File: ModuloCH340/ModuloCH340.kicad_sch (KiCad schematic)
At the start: 20 parts, among them J1001 USB_C_Receptacle_USB2.0, J1002 USB_B, J1003 Conn_01x04, U1001 CH340G, Y1001 12Mhz

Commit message: Some changes in arduino board.
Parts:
- renumbered C1001 to C13, C1002 to C14, C1003 to C15, C1004 to C16, D1001 to D3, D1002 to D4, J1001 to J11, J1002 to J12, J1003 to J13, JP1001 to JP1, R1006 to R10, R1007 to R11, R1008 to R12, R1001 to R5, R1002 to R6, R1003 to R7, R1004 to R8, R1005 to R9, U1001 to U3, Y1001 to Y2
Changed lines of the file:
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@@
 		(on_board yes)
 		(dnp no)
-		(property "Reference" "R1007"
+		(property "Reference" "R11"
 			(at 201.422 115.824 0)
 			(effects
@@
 				)
 			)
+			(project "ModuloCH340"
+				(path "/b1260de1-9c48-4b08-a759-f31e40d6183e/17bee45f-f3a2-49e1-a0f6-7717cbcaab1c"
+					(reference "R11")
+					(unit 1)
+				)
+			)
 		)
 	)
@@
 		(dnp no)
 		(fields_autoplaced yes)
-		(property "Reference" "R1002"
+		(property "Reference" "R6"
 			(at 121.92 76.1999 0)
 			(effects
@@
 				)
 			)
+			(project "ModuloCH340"
+				(path "/b1260de1-9c48-4b08-a759-f31e40d6183e/17bee45f-f3a2-49e1-a0f6-7717cbcaab1c"
+					(reference "R6")
+					(unit 1)
+				)
+			)
 		)
 	)
@@
 		(dnp no)
 		(fields_autoplaced yes)
-		(property "Reference" "R1001"
+		(property "Reference" "R5"
 			(at 113.03 76.1999 0)
 			(effects
@@
 				)
 			)
+			(project ""
+				(path "/b1260de1-9c48-4b08-a759-f31e40d6183e/17bee45f-f3a2-49e1-a0f6-7717cbcaab1c"
+					(reference "R5")
+					(unit 1)
+				)
+			)
 		)
 	)
@@
 		(on_board yes)
 		(dnp no)
-		(property "Reference" "Y1001"
+		(property "Reference" "Y2"
 			(at 125.476 118.11 0)
 			(effects
@@
 				(path "/49c4e1fc-25c5-4450-b617-b77ec3b06c82"
 					(reference "Y1001")
+					(unit 1)
+				)
+			)
+			(project ""
+				(path "/b1260de1-9c48-4b08-a759-f31e40d6183e/17bee45f-f3a2-49e1-a0f6-7717cbcaab1c"
+					(reference "Y2")
 					(unit 1)
 				)
@@
 		(dnp no)
 		(fields_autoplaced yes)
-		(property "Reference" "C1003"
+		(property "Reference" "C15"
 			(at 168.91 68.5862 0)
 			(effects
@@
 				)
 			)
+			(project ""
+				(path "/b1260de1-9c48-4b08-a759-f31e40d6183e/17bee45f-f3a2-49e1-a0f6-7717cbcaab1c"
+					(reference "C15")
+					(unit 1)
+				)
+			)
 		)
 	)
@@
 		(on_board yes)
 		(dnp no)
-		(property "Reference" "C1001"
+		(property "Reference" "C13"
 			(at 123.698 127.508 0)
 			(effects
@@
 				)
 			)
+			(project "ModuloCH340"
+				(path "/b1260de1-9c48-4b08-a759-f31e40d6183e/17bee45f-f3a2-49e1-a0f6-7717cbcaab1c"
+					(reference "C13")
+					(unit 1)
+				)
+			)
 		)
 	)
@@
 		(dnp no)
 		(fields_autoplaced yes)
-		(property "Reference" "C1004"
+		(property "Reference" "C16"
 			(at 214.63 80.0162 0)
 			(effects
@@
 				)
 			)
+			(project "ModuloCH340"
+				(path "/b1260de1-9c48-4b08-a759-f31e40d6183e/17bee45f-f3a2-49e1-a0f6-7717cbcaab1c"
+					(reference "C16")
+					(unit 1)
+				)
+			)
 		)
 	)
@@
 		(dnp no)
 		(fields_autoplaced yes)
-		(property "Reference" "R1005"
+		(property "Reference" "R9"
 			(at 185.42 85.09 90)
 			(effects
@@
 				)
 			)
+			(project "ModuloCH340"
+				(path "/b1260de1-9c48-4b08-a759-f31e40d6183e/17bee45f-f3a2-49e1-a0f6-7717cbcaab1c"
+					(reference "R9")
+					(unit 1)
+				)
+			)
 		)
 	)
@@
 		(dnp no)
 		(fields_autoplaced yes)
-		(property "Reference" "J1003"
+		(property "Reference" "J13"
 			(at 180.34 100.3299 0)
 			(effects
@@
 				)
 			)
+			(project ""
+				(path "/b1260de1-9c48-4b08-a759-f31e40d6183e/17bee45f-f3a2-49e1-a0f6-7717cbcaab1c"
+					(reference "J13")
+					(unit 1)
+				)
+			)
 		)
 	)
@@
 		(on_board yes)
 		(dnp no)
-		(property "Reference" "R1004"
+		(property "Reference" "R8"
 			(at 132.08 102.87 90)
 			(effects
@@
 				)
 			)
+			(project "ModuloCH340"
+				(path "/b1260de1-9c48-4b08-a759-f31e40d6183e/17bee45f-f3a2-49e1-a0f6-7717cbcaab1c"
+					(reference "R8")
+					(unit 1)
+				)
+			)
 		)
 	)
@@
 		(dnp no)
 		(fields_autoplaced yes)
-		(property "Reference" "J1001"
+		(property "Reference" "J11"
 			(at 83.82 57.15 0)
 			(effects
@@
 				)
 			)
+			(project ""
+				(path "/b1260de1-9c48-4b08-a759-f31e40d6183e/17bee45f-f3a2-49e1-a0f6-7717cbcaab1c"
+					(reference "J11")
+					(unit 1)
+				)
+			)
 		)
 	)
@@
 		(dnp no)
 		(fields_autoplaced yes)
-		(property "Reference" "J1002"
+		(property "Reference" "J12"
 			(at 88.9 109.22 0)
 			(effects
@@
 				)
 			)
+			(project ""
+				(path "/b1260de1-9c48-4b08-a759-f31e40d6183e/17bee45f-f3a2-49e1-a0f6-7717cbcaab1c"
+					(reference "J12")
+					(unit 1)
+				)
+			)
 		)
 	)
@@
 		(dnp no)
 		(fields_autoplaced yes)
-		(property "Reference" "R1003"
+		(property "Reference" "R7"
 			(at 132.08 92.71 90)
 			(effects
@@
 				)
 			)
+			(project "ModuloCH340"
+				(path "/b1260de1-9c48-4b08-a759-f31e40d6183e/17bee45f-f3a2-49e1-a0f6-7717cbcaab1c"
+					(reference "R7")
+					(unit 1)
+				)
+			)
 		)
 	)
@@
 		(dnp no)
 		(fields_autoplaced yes)
-		(property "Reference" "JP1001"
+		(property "Reference" "JP1"
 			(at 111.76 58.42 0)
 			(effects
@@
 				)
 			)
+			(project ""
+				(path "/b1260de1-9c48-4b08-a759-f31e40d6183e/17bee45f-f3a2-49e1-a0f6-7717cbcaab1c"
+					(reference "JP1")
+					(unit 1)
+				)
+			)
 		)
 	)
@@
 		(on_board yes)
 		(dnp no)
-		(property "Reference" "R1008"
+		(property "Reference" "R12"
 			(at 215.392 115.824 0)
 			(effects
@@
 				)
 			)
+			(project "ModuloCH340"
+				(path "/b1260de1-9c48-4b08-a759-f31e40d6183e/17bee45f-f3a2-49e1-a0f6-7717cbcaab1c"
+					(reference "R12")
+					(unit 1)
+				)
+			)
 		)
 	)
@@
 		(dnp no)
 		(fields_autoplaced yes)
-		(property "Reference" "D1002"
+		(property "Reference" "D4"
 			(at 214.63 107.8864 90)
 			(effects
@@
 				)
 			)
+			(project "ModuloCH340"
+				(path "/b1260de1-9c48-4b08-a759-f31e40d6183e/17bee45f-f3a2-49e1-a0f6-7717cbcaab1c"
+					(reference "D4")
+					(unit 1)
+				)
+			)
 		)
 	)
@@
 		(dnp no)
 		(fields_autoplaced yes)
-		(property "Reference" "U1001"
+		(property "Reference" "U3"
 			(at 162.1633 115.57 0)
 			(effects
@@
 				)
 			)
+			(project ""
+				(path "/b1260de1-9c48-4b08-a759-f31e40d6183e/17bee45f-f3a2-49e1-a0f6-7717cbcaab1c"
+					(reference "U3")
+					(unit 1)
+				)
+			)
 		)
 	)
@@
 		(dnp no)
 		(fields_autoplaced yes)
-		(property "Reference" "D1001"
+		(property "Reference" "D3"
 			(at 200.66 107.8864 90)
 			(effects
@@
 				)
 			)
+			(project ""
+				(path "/b1260de1-9c48-4b08-a759-f31e40d6183e/17bee45f-f3a2-49e1-a0f6-7717cbcaab1c"
+					(reference "D3")
+					(unit 1)
+				)
+			)
 		)
 	)
@@
 		(dnp no)
 		(fields_autoplaced yes)
-		(property "Reference" "C1002"
+		(property "Reference" "C14"
 			(at 149.86 127.0062 0)
 			(effects
@@
 				)
 			)
+			(project "ModuloCH340"
+				(path "/b1260de1-9c48-4b08-a759-f31e40d6183e/17bee45f-f3a2-49e1-a0f6-7717cbcaab1c"
+					(reference "C14")
+					(unit 1)
+				)
+			)
 		)
 	)
@@
 		(on_board yes)
 		(dnp no)
-		(property "Reference" "R1006"
+		(property "Reference" "R10"
 			(at 185.42 95.25 90)
 			(effects
@@
 				)
 			)
-		)
-	)
-	(sheet_instances
-		(path "/"
-			(page "1")
-		)
-	)
-	(embedded_fonts no)
+			(project "ModuloCH340"
+				(path "/b1260de1-9c48-4b08-a759-f31e40d6183e/17bee45f-f3a2-49e1-a0f6-7717cbcaab1c"
+					(reference "R10")
+					(unit 1)
+				)
+			)
+		)
+	)
 )

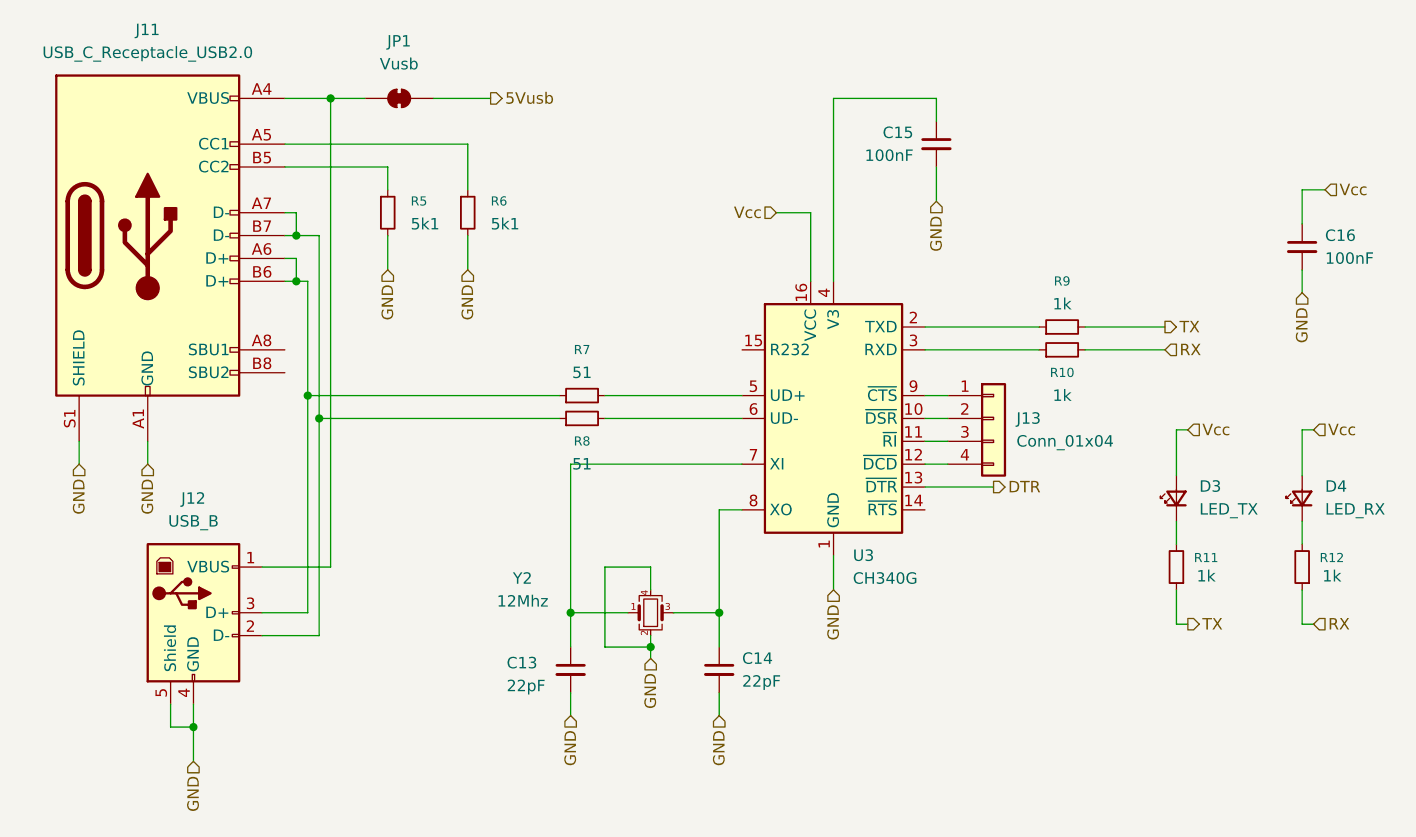
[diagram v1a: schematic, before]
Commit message: Added all components to arduino pcb.
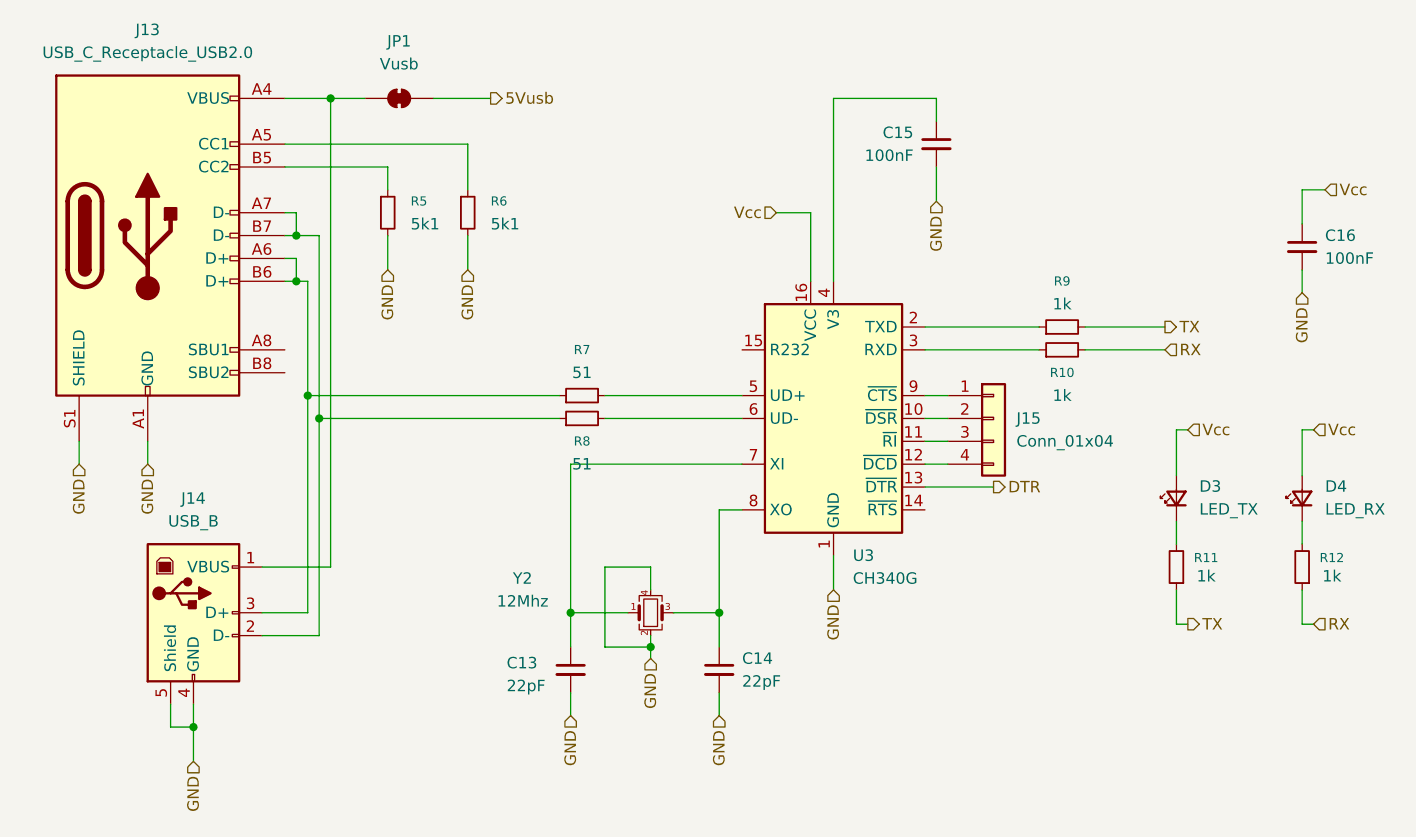
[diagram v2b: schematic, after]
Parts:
- C13, C14, C15, C16: footprint Capacitor_SMD:C_0805_2012Metric -> Capacitor_SMD:C_0805_2012Metric_Pad1.18x1.45mm_HandSolder
- R10, R11, R12, R5, R6, R7, R8, R9: footprint Resistor_SMD:R_0805_2012Metric -> Resistor_SMD:R_0805_2012Metric_Pad1.20x1.40mm_HandSolder
- renumbered J11 to J13, J12 to J14, J13 to J15
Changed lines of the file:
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@@
 			)
 		)
-		(property "Footprint" "Resistor_SMD:R_0805_2012Metric"
+		(property "Footprint" "Resistor_SMD:R_0805_2012Metric_Pad1.20x1.40mm_HandSolder"
 			(at 198.12 116.84 0)
 			(effects
@@
 			)
 		)
-		(property "Footprint" "Resistor_SMD:R_0805_2012Metric"
+		(property "Footprint" "Resistor_SMD:R_0805_2012Metric_Pad1.20x1.40mm_HandSolder"
 			(at 119.38 77.47 0)
 			(effects
@@
 			)
 		)
-		(property "Footprint" "Resistor_SMD:R_0805_2012Metric"
+		(property "Footprint" "Resistor_SMD:R_0805_2012Metric_Pad1.20x1.40mm_HandSolder"
 			(at 110.49 77.47 0)
 			(effects
@@
 			)
 		)
-		(property "Footprint" "Capacitor_SMD:C_0805_2012Metric"
+		(property "Footprint" "Capacitor_SMD:C_0805_2012Metric_Pad1.18x1.45mm_HandSolder"
 			(at 171.45 69.85 0)
 			(effects
@@
 			)
 		)
-		(property "Footprint" "Capacitor_SMD:C_0805_2012Metric"
+		(property "Footprint" "Capacitor_SMD:C_0805_2012Metric_Pad1.18x1.45mm_HandSolder"
 			(at 130.81 128.27 0)
 			(effects
@@
 			)
 		)
-		(property "Footprint" "Capacitor_SMD:C_0805_2012Metric"
+		(property "Footprint" "Capacitor_SMD:C_0805_2012Metric_Pad1.18x1.45mm_HandSolder"
 			(at 212.09 81.28 0)
 			(effects
@@
 			)
 		)
-		(property "Footprint" "Resistor_SMD:R_0805_2012Metric"
+		(property "Footprint" "Resistor_SMD:R_0805_2012Metric_Pad1.20x1.40mm_HandSolder"
 			(at 185.42 90.17 0)
 			(effects
@@
 		(dnp no)
 		(fields_autoplaced yes)
-		(property "Reference" "J13"
+		(property "Reference" "J15"
 			(at 180.34 100.3299 0)
 			(effects
@@
 			(project ""
 				(path "/b1260de1-9c48-4b08-a759-f31e40d6183e/17bee45f-f3a2-49e1-a0f6-7717cbcaab1c"
-					(reference "J13")
+					(reference "J15")
 					(unit 1)
 				)
@@
 			)
 		)
-		(property "Footprint" "Resistor_SMD:R_0805_2012Metric"
+		(property "Footprint" "Resistor_SMD:R_0805_2012Metric_Pad1.20x1.40mm_HandSolder"
 			(at 132.08 100.33 0)
 			(effects
@@
 		(dnp no)
 		(fields_autoplaced yes)
-		(property "Reference" "J11"
+		(property "Reference" "J13"
 			(at 83.82 57.15 0)
 			(effects
@@
 			(project ""
 				(path "/b1260de1-9c48-4b08-a759-f31e40d6183e/17bee45f-f3a2-49e1-a0f6-7717cbcaab1c"
-					(reference "J11")
+					(reference "J13")
 					(unit 1)
 				)
@@
 		(dnp no)
 		(fields_autoplaced yes)
-		(property "Reference" "J12"
+		(property "Reference" "J14"
 			(at 88.9 109.22 0)
 			(effects
@@
 			(project ""
 				(path "/b1260de1-9c48-4b08-a759-f31e40d6183e/17bee45f-f3a2-49e1-a0f6-7717cbcaab1c"
-					(reference "J12")
+					(reference "J14")
 					(unit 1)
 				)
@@
 			)
 		)
-		(property "Footprint" "Resistor_SMD:R_0805_2012Metric"
+		(property "Footprint" "Resistor_SMD:R_0805_2012Metric_Pad1.20x1.40mm_HandSolder"
 			(at 132.08 97.79 0)
 			(effects
@@
 			)
 		)
-		(property "Footprint" "Resistor_SMD:R_0805_2012Metric"
+		(property "Footprint" "Resistor_SMD:R_0805_2012Metric_Pad1.20x1.40mm_HandSolder"
 			(at 212.09 116.84 0)
 			(effects
@@
 			)
 		)
-		(property "Footprint" "Capacitor_SMD:C_0805_2012Metric"
+		(property "Footprint" "Capacitor_SMD:C_0805_2012Metric_Pad1.18x1.45mm_HandSolder"
 			(at 147.32 128.27 0)
 			(effects
@@
 			)
 		)
-		(property "Footprint" "Resistor_SMD:R_0805_2012Metric"
+		(property "Footprint" "Resistor_SMD:R_0805_2012Metric_Pad1.20x1.40mm_HandSolder"
 			(at 185.42 92.71 0)
 			(effects

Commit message: First version from PCB schematic.
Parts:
- renumbered JP1 to JP2
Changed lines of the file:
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@@
 		(dnp no)
 		(fields_autoplaced yes)
-		(property "Reference" "JP1"
+		(property "Reference" "JP2"
 			(at 111.76 58.42 0)
 			(effects
@@
 			(project ""
 				(path "/b1260de1-9c48-4b08-a759-f31e40d6183e/17bee45f-f3a2-49e1-a0f6-7717cbcaab1c"
-					(reference "JP1")
+					(reference "JP2")
 					(unit 1)
 				)
